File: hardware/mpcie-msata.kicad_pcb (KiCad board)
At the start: 4 copper layers, 100 x 85 mm, 205 parts, among them J102 TNG-Power-BTM, J103 TNG-Power-TOP, J104 TNG-Data-BTM, J105 TNG-Data-TOP, J201 Mini-PCIE, J202 SIM8060, J301 Mini-SATA, P101 Debug, P102 PE, Q301 40MHz, SW101 BOOT, U101 USB2514B, U102 LD1117, U103 TPS7A7002, U104 STM32F070CBT6, U105 82400152, U201 LM813, U301 TUSB9261PVP, U302 TLV71211DBVR, U303 AP7333-18SAG-7, U304 AT25DF011-SSHN-T, X101 24MHz, X102 TBD

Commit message: fix values
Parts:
- R114: value 510 -> 1k

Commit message: add hints
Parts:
- R310: value DNP -> 0
- R313: value 10k -> DNP
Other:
- board text added: "More distance to connector"
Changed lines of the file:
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@@
   (general
     (thickness 1.6)
-    (drawings 15)
+    (drawings 16)
     (tracks 2816)
     (zones 0)
@@
       (effects (font (size 0.2 0.2) (thickness 0.05)) (justify mirror))
     )
-    (fp_text value DNP (at 0 0.15 90) (layer B.Fab)
+    (fp_text value 0 (at 0 0.15 90) (layer B.Fab)
       (effects (font (size 0.2 0.2) (thickness 0.05)) (justify mirror))
     )
@@
       (effects (font (size 0.2 0.2) (thickness 0.05)) (justify mirror))
     )
-    (fp_text value 10k (at 0 0.15) (layer B.Fab)
+    (fp_text value DNP (at 0 0.15) (layer B.Fab)
       (effects (font (size 0.2 0.2) (thickness 0.05)) (justify mirror))
     )
@@
     )
   )
+  (gr_text "More distance to connector" (at 107.45 66.95) (layer Dwgs.User)
+    (effects (font (size 1.5 1.5) (thickness 0.3)))
+  )
   (gr_text "Mini SATA" (at 110.05 84.1 90) (layer F.SilkS)

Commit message: add version 1.1
 * fix footprints
 * remove lm813
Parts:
- removed C145: >100uF, ELKO_63
- removed C208: 10uF, C0805
- removed L104: 744230900, WE-CNSW-0603
- removed L110: INDUCTs, kicad-libraries:R0805E
- removed R107: DNP, R0402F
- removed R117: 10k, R0402F
- removed R205, R206, R207: 1k, kicad-libraries:R0402F
- removed RP202: 1k, kicad-libraries:4X0402
- removed U201: LM813, kicad-libraries:LM813
- added Q101: 2N7002, kicad-libraries:SOT23GDS, F.Cu at (104.2, 54.9)
- C148, C150, C151, C202: value >100uF -> 100uF
- C310, C311, C312, C313: footprint kicad-libraries:C0402E -> kicad-libraries:C0402F
- R111: value DNP -> 10k
- moved R106 12.5 mm to (105.7, 57.1)
- moved C129 11.7 mm to (105.1, 59.2)
- moved C127 11.7 mm to (102.4, 67.9)
- moved P101 11.7 mm to (99.8, 60.4)
- moved C123 11.7 mm to (93.0, 58.7)
- moved C130 11.7 mm to (97.0, 56.5)
- moved C131 11.7 mm to (94.0, 58.7)
- moved C124 11.7 mm to (93.5, 64.6)
- moved C133 11.7 mm to (93.9, 63.1)
- moved C137 11.7 mm to (89.4, 61.6)
- moved C138 11.7 mm to (91.5, 64.1)
- moved C139 11.7 mm to (90.0, 65.8)
- moved L108 11.7 mm to (93.2, 65.8)
- moved U104 11.7 mm to (99.5, 62.1)
- moved X102 11.7 mm to (91.5, 61.6)
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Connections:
- net Net-(R114-Pad2) renamed BOOT
- J102 pad 21: (no net) -> Net-(J102-Pad21)
- J102 pad 22: (no net) -> Net-(J102-Pad22)
- J102 pad 23: (no net) -> Net-(J102-Pad23)
- J102 pad 24: (no net) -> Net-(J102-Pad24)
- J102 pad 25: (no net) -> Net-(J102-Pad25)
- J102 pad 26: (no net) -> Net-(J102-Pad26)
- J102 pad 27: (no net) -> Net-(J102-Pad27)
- J102 pad 28: (no net) -> Net-(J102-Pad28)
- J102 pad 29: (no net) -> Net-(J102-Pad29)
- J102 pad 30: (no net) -> Net-(J102-Pad30)
- J103 pad 21: (no net) -> Net-(J103-Pad21)
- J103 pad 22: (no net) -> Net-(J103-Pad22)
- J103 pad 23: (no net) -> Net-(J103-Pad23)
- J103 pad 24: (no net) -> Net-(J103-Pad24)
- J103 pad 25: (no net) -> Net-(J103-Pad25)
- J103 pad 26: (no net) -> Net-(J103-Pad26)
- J103 pad 27: (no net) -> Net-(J103-Pad27)
- J103 pad 28: (no net) -> Net-(J103-Pad28)
- J103 pad 29: (no net) -> Net-(J103-Pad29)
- J103 pad 30: (no net) -> Net-(J103-Pad30)
- J105 pad 35: (no net) -> Net-(J105-Pad35)
- J105 pad 37: (no net) -> Net-(J105-Pad37)
- J201 pad 1: (no net) -> Net-(J201-Pad1)
- J201 pad 11: (no net) -> Net-(J201-Pad11)
- J201 pad 13: (no net) -> Net-(J201-Pad13)
- J201 pad 17: (no net) -> Net-(J201-Pad17)
- J201 pad 23: (no net) -> Net-(J201-Pad23)
- J201 pad 25: (no net) -> Net-(J201-Pad25)
- J201 pad 28: (no net) -> Net-(J201-Pad28)
- J201 pad 3: (no net) -> Net-(J201-Pad3)
- J201 pad 30: (no net) -> Net-(J201-Pad30)
- J201 pad 31: (no net) -> Net-(J201-Pad31)
- J201 pad 32: (no net) -> Net-(J201-Pad32)
- J201 pad 33: (no net) -> Net-(J201-Pad33)
- J201 pad 45: (no net) -> Net-(J201-Pad45)
- J201 pad 47: (no net) -> Net-(J201-Pad47)
- J201 pad 48: (no net) -> Net-(J201-Pad48)
- J201 pad 49: (no net) -> Net-(J201-Pad49)
- J201 pad 5: (no net) -> Net-(J201-Pad5)
- J201 pad 51: (no net) -> Net-(J201-Pad51)
- J201 pad 6: (no net) -> Net-(J201-Pad6)
- J201 pad 7: (no net) -> Net-(J201-Pad7)
- J301 pad 1: (no net) -> Net-(J301-Pad1)
- J301 pad 10: (no net) -> Net-(J301-Pad10)
- J301 pad 11: (no net) -> Net-(J301-Pad11)
- J301 pad 12: (no net) -> Net-(J301-Pad12)
- J301 pad 13: (no net) -> Net-(J301-Pad13)
- J301 pad 14: (no net) -> Net-(J301-Pad14)
- J301 pad 16: (no net) -> Net-(J301-Pad16)
- J301 pad 17: (no net) -> Net-(J301-Pad17)
- J301 pad 19: (no net) -> Net-(J301-Pad19)
- J301 pad 20: (no net) -> Net-(J301-Pad20)
- J301 pad 22: (no net) -> Net-(J301-Pad22)
- J301 pad 28: (no net) -> Net-(J301-Pad28)
- J301 pad 3: (no net) -> Net-(J301-Pad3)
- J301 pad 30: (no net) -> Net-(J301-Pad30)
- J301 pad 32: (no net) -> Net-(J301-Pad32)
- J301 pad 36: (no net) -> Net-(J301-Pad36)
- J301 pad 38: (no net) -> Net-(J301-Pad38)
- J301 pad 42: (no net) -> Net-(J301-Pad42)
- J301 pad 43: (no net) -> Net-(J301-Pad43)
- J301 pad 44: (no net) -> Net-(J301-Pad44)
- J301 pad 45: (no net) -> Net-(J301-Pad45)
- J301 pad 46: (no net) -> Net-(J301-Pad46)
- J301 pad 47: (no net) -> Net-(J301-Pad47)
- J301 pad 48: (no net) -> Net-(J301-Pad48)
- J301 pad 5: (no net) -> Net-(J301-Pad5)
- J301 pad 51: (no net) -> Net-(J301-Pad51)
- J301 pad 6: (no net) -> Net-(J301-Pad6)
- J301 pad 7: (no net) -> Net-(J301-Pad7)
- J301 pad 8: (no net) -> Net-(J301-Pad8)
- R109 pad 2: 3V3 -> GND
- RP201 pad 3: (no net) -> Net-(RP201-Pad3)
- RP201 pad 6: (no net) -> Net-(RP201-Pad6)
- RP301 pad 2: (no net) -> Net-(RP301-Pad2)
- RP301 pad 3: (no net) -> Net-(RP301-Pad3)
- RP301 pad 6: (no net) -> Net-(RP301-Pad6)
- RP301 pad 7: (no net) -> Net-(RP301-Pad7)
- U101 pad 12: (no net) -> Net-(U101-Pad12)
- U101 pad 16: (no net) -> Net-(U101-Pad16)
- U101 pad 18: (no net) -> Net-(U101-Pad18)
- U101 pad 20: (no net) -> Net-(U101-Pad20)
- U103 pad 5: (no net) -> Net-(U103-Pad5)
- U104 pad 10: LM813_LED_WL -> Net-(U104-Pad10)
- U104 pad 11: LM813_WLAN_DIS -> Net-(U104-Pad11)
- U104 pad 2: LM813_BT_DIS -> Net-(U104-Pad2)
- U104 pad 28: (no net) -> Net-(U104-Pad28)
- U104 pad 3: LM813_LED_BT -> Net-(U104-Pad3)
- U104 pad 38: (no net) -> Net-(U104-Pad38)
- U104 pad 39: (no net) -> Net-(U104-Pad39)
- U104 pad 4: LM813_BT_WAKE_HOST -> Net-(U104-Pad4)
- U104 pad 41: (no net) -> Net-(U104-Pad41)
- U104 pad 42: (no net) -> Net-(U104-Pad42)
- U104 pad 46: LM813_EN -> Net-(U104-Pad46)
- U104 pad 7: (no net) -> Net-(U104-Pad7)
- U301 pad 10: (no net) -> Net-(U301-Pad10)
- U301 pad 11: (no net) -> Net-(U301-Pad11)
- U301 pad 13: (no net) -> Net-(U301-Pad13)
- U301 pad 14: (no net) -> Net-(U301-Pad14)
- U301 pad 15: (no net) -> Net-(U301-Pad15)
- U301 pad 16: (no net) -> Net-(U301-Pad16)
- U301 pad 22: (no net) -> Net-(U301-Pad22)
- U301 pad 23: (no net) -> Net-(U301-Pad23)
- U301 pad 25: (no net) -> Net-(U301-Pad25)
- U301 pad 26: (no net) -> Net-(U301-Pad26)
- U301 pad 27: (no net) -> Net-(U301-Pad27)
- U301 pad 28: (no net) -> Net-(U301-Pad28)
- U301 pad 37: (no net) -> Net-(U301-Pad37)
- U301 pad 42: (no net) -> Net-(U301-Pad42)
- U301 pad 43: (no net) -> Net-(U301-Pad43)
- U301 pad 45: (no net) -> Net-(U301-Pad45)
- U301 pad 46: (no net) -> Net-(U301-Pad46)
- U301 pad 54: (no net) -> Net-(U301-Pad54)
- U301 pad 64: (no net) -> Net-(U301-Pad64)
- U301 pad 8: (no net) -> Net-(U301-Pad8)
- U301 pad 9: (no net) -> Net-(U301-Pad9)
- U302 pad 4: (no net) -> Net-(U302-Pad4)
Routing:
- net 5V: track 162.2 -> 0.00 mm, vias 12 -> 0
- net 3V3: track 212.6 -> 101.5 mm, vias 31 -> 29
- net LM813_DM: track 39.6 -> 0.00 mm, vias 1 -> 0
- net LM813_DP: track 37.1 -> 0.00 mm, vias 1 -> 0
- net LM813_EN: track 30.6 -> 0.00 mm, vias 2 -> 0
- net LM813_WLAN_DIS: track 26.5 -> 0.00 mm, vias 2 -> 0
- net LM813_BT_DIS: track 24.6 -> 0.00 mm, vias 2 -> 0
- net Net-(RP202-Pad3): track 20.4 -> 0.00 mm, vias 1 -> 0
- net LM813_LED_BT: track 15.4 -> 0.00 mm, vias 1 -> 0
- net GND: track 389.5 -> 374.7 mm, vias 285 -> 270
- net MPCIE_LED_WPAN: track 34.9 -> 49.0 mm
- net MPCIE_LED_WWAN: track 34.7 -> 48.7 mm
- net MPCIE_LED_WIFI: track 34.8 -> 48.8 mm
- net MSATA_TX: track 41.4 -> 55.2 mm
- net MPCIE_#RESET: track 52.4 -> 66.2 mm
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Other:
- board text added: "Copyright Tinkerforge GmbH 2020. This documentation describes Open Hardware and is licensed under the CERN OHL v. 1.1. You may redistribute and modify this documentation under the terms of the CERN OHL v.1.1. (http://ohwr.org/cernohl). This documentation is distributed WITHOUT ANY EXPRESS OR IMPLIED WARRANTY, INCLUDING OF MERCHANTABILITY, SATISFACTORY QUALITY AND FITNESS FOR A PARTICULAR PURPOSE.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"
- board text added: "MPCIE-MSATA REV 1.1"
- board text removed: "MPCIE-MSATA-WIFI/BT REV 1.0"
- board text removed: "More distance to connector"

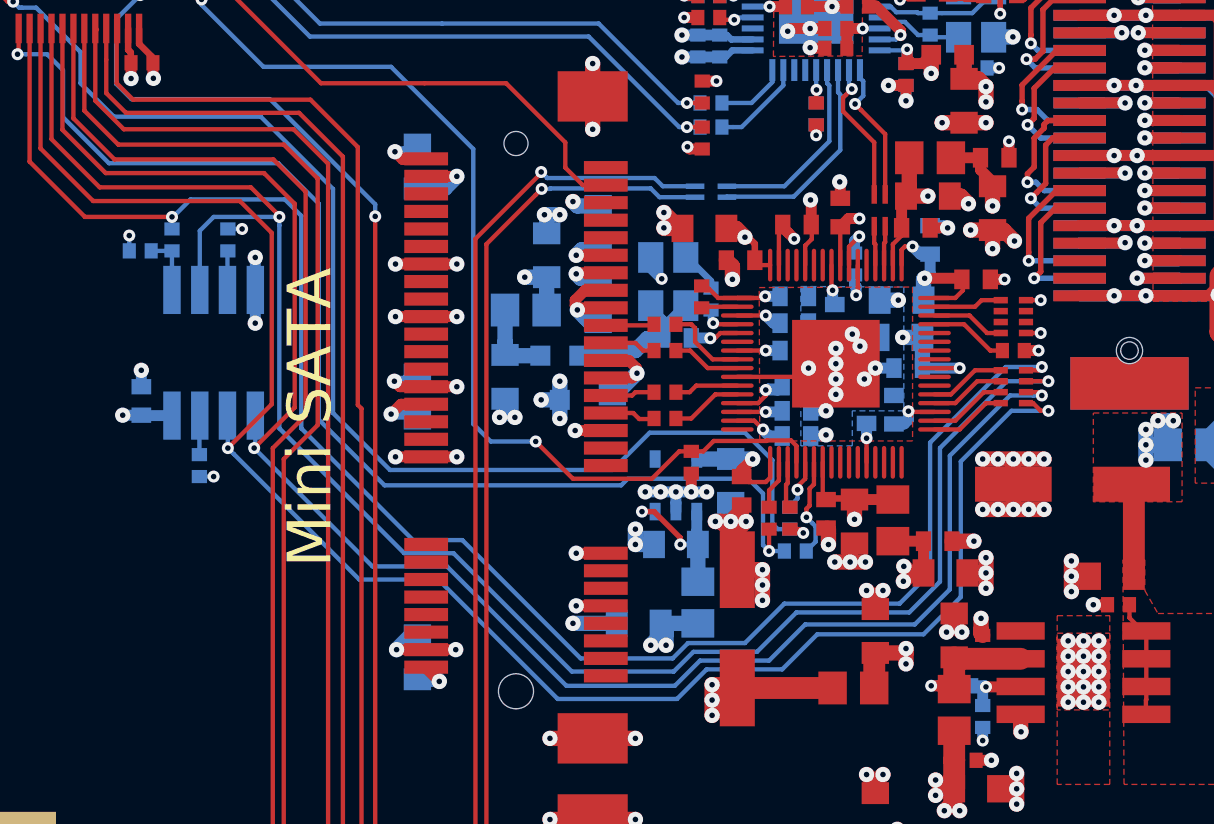
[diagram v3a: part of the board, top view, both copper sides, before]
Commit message: fix footprints
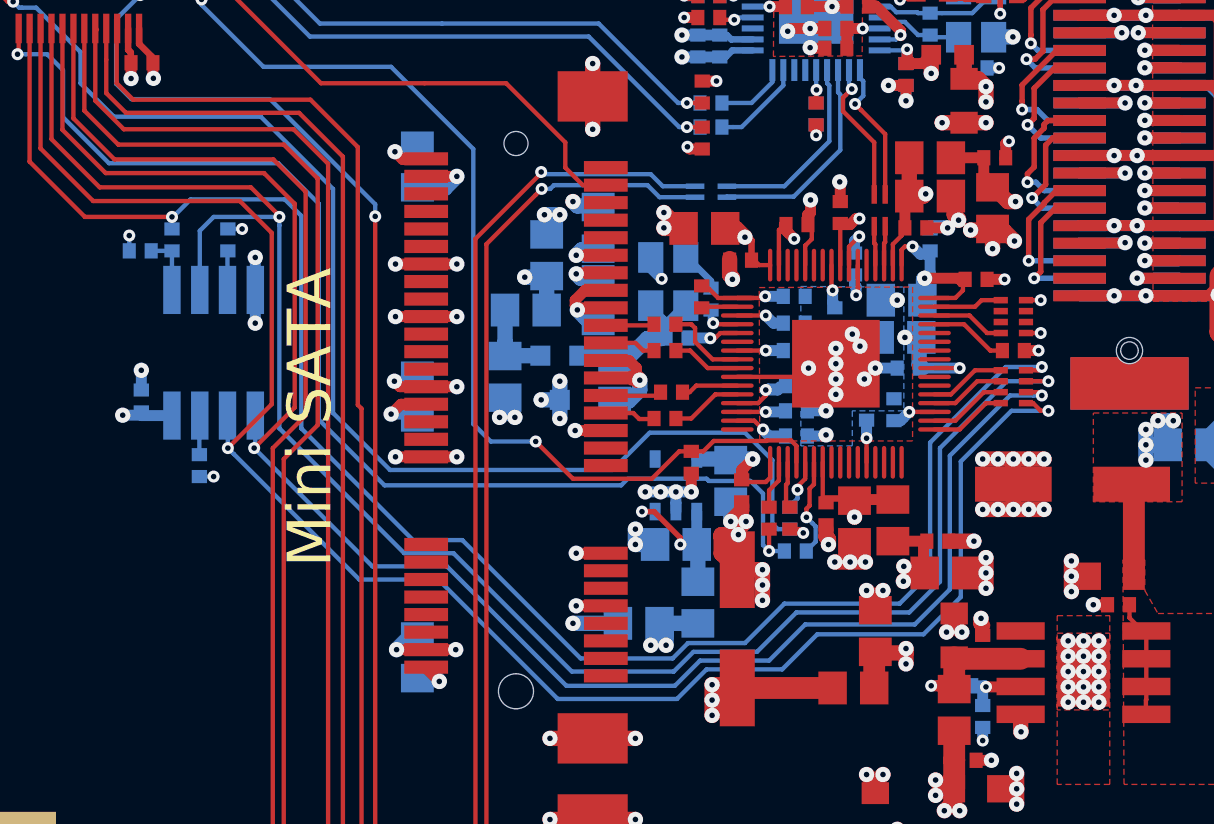
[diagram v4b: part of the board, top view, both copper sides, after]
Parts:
- C121, C122: value TBD/47pF -> 47pF
- C137, C138: value TBD -> 33pF
- C301, C302, C303, C304, C305, C309, C325, C326, C327, C328, C329, C330, C331, C339, C340, C341, C342, C345, C346: footprint C0805 -> kicad-libraries:C0805E
- C306: value >100uF -> 100uF
- C308, C314, C315, C316, C317, C318, C319, C320, C321, C322, C323, C324, C332, C333, C334, C335, C336, C337, C338, C343, C344, C347: footprint kicad-libraries:C0402E -> kicad-libraries:C0402F
- X102: value TBD -> 8MHz
- moved C326 0.36 mm to (124.0, 82.4)
- moved C312 0.30 mm to (126.5, 83.0)
- moved C342 0.10 mm to (138.3, 74.0)
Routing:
- net GND: track 374.7 -> 374.2 mm, vias 270 -> 269

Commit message: fix name
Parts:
- U304: value AT25DF011-SSHN-T -> AT25DF011-SSHN-T

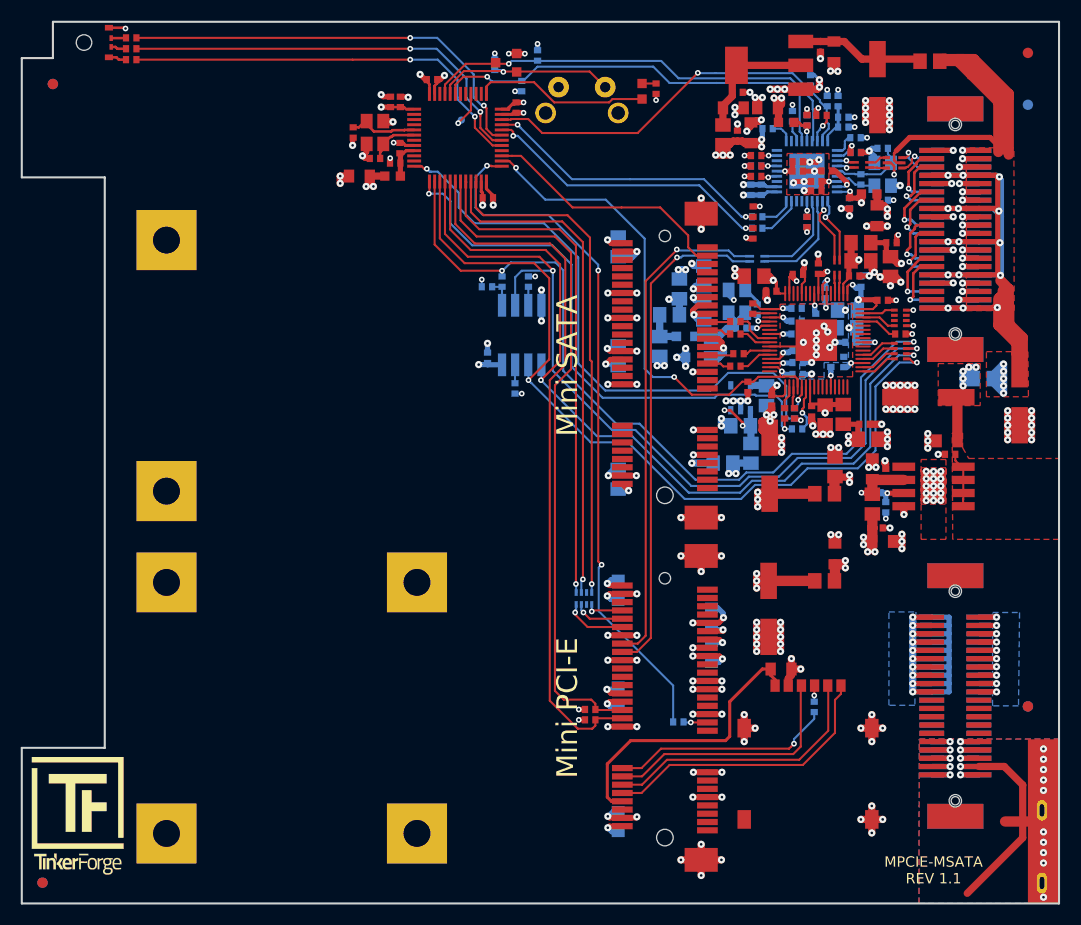
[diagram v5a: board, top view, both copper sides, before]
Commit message: fix footprints
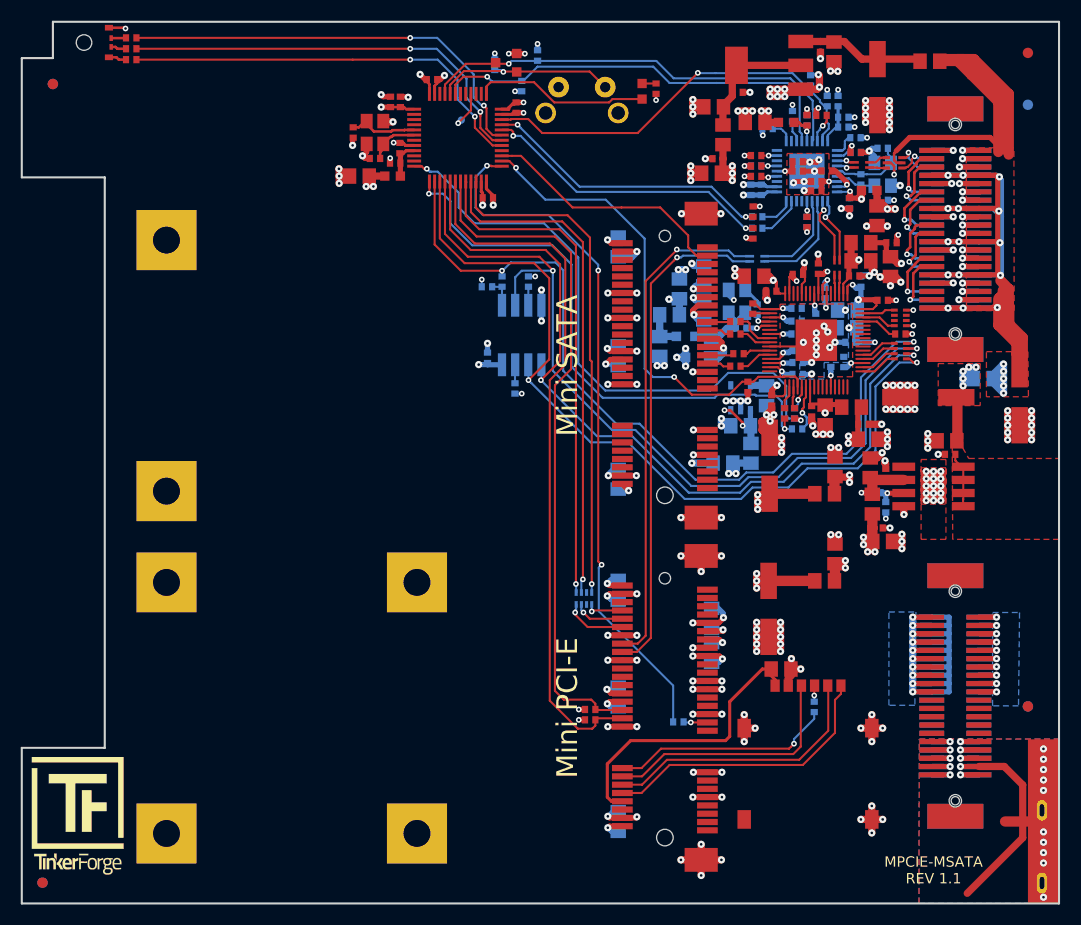
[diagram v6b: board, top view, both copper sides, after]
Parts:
- C116, C125, C128, C132, C136, C139, C140, C146, C147, C201, C203, C204, C205, C206, C207, C209: footprint C0805 -> kicad-libraries:C0805E
- moved C128 5.45 mm to (124.0, 65.5), turned to 180 degrees
- moved C134 2.91 mm to (124.5, 64.2), turned to 180 degrees
- moved C136 1.90 mm to (124.2, 59.1), turned to 180 degrees
- moved C116 1.84 mm to (128.2, 60.6)
- moved L304 1.06 mm to (137.4, 88.1), turned to 180 degrees
- moved L103 0.35 mm to (139.2, 67.2)
- moved C140 0.22 mm to (139.2, 94.0)
- moved C343 0.10 mm to (138.6, 89.8)
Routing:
- net GND: track 374.2 -> 379.8 mm, vias 269 -> 275
- net 3V3: track 101.5 -> 98.5 mm, vias 29 -> 28

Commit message: fix names
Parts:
- U302: value TLV71211DBVR -> TLV71211DBVR
- U303: value AP7333-18SAG-7 -> AP7333-18SAG-7

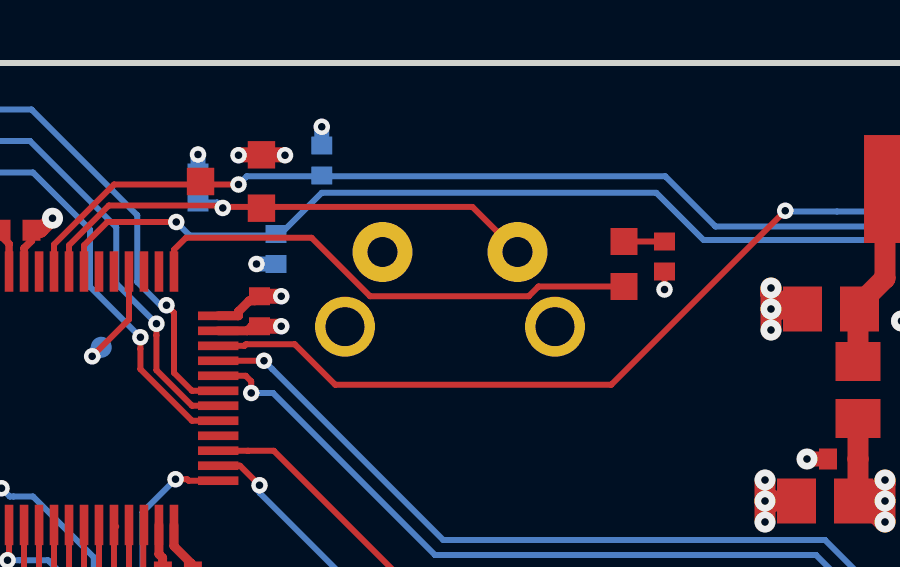
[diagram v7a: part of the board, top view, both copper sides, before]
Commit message: all footprints updated
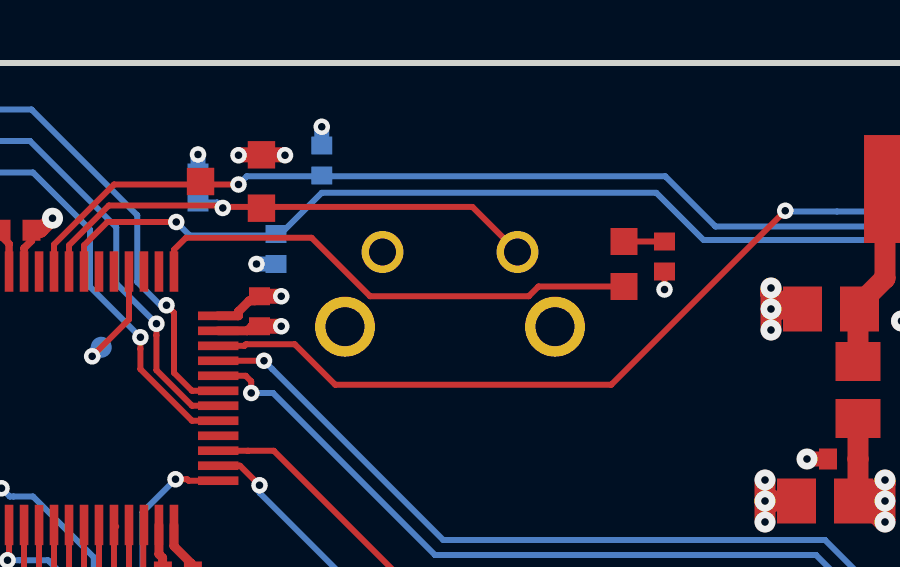
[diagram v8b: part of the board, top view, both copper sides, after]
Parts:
- C101, C102, C103, C104, C105, C106, C107, C108, C109, C110, C111, C112, C113, C114, C115, C117, C118, C119, C120, C121, C122, C123, C124, C126, C127, C129, C130, C131, C133, C134, C135, C137, C138, C141, C142, C143, C144: footprint C0402F -> kicad-libraries:C0402F
- C148, C150, C151, C202, C306: footprint ELKO_63 -> kicad-libraries:ELKO_63
- D102: footprint D0603F -> kicad-libraries:D0603F
- J102, J104: footprint TNG-40-BTM -> kicad-libraries:TNG-40-BTM
- J103, J105: footprint TNG-40-TOP -> kicad-libraries:TNG-40-TOP
- L101, L103, L108: footprint R0603F -> kicad-libraries:R0603F
- L102, L105: footprint WE-CNSW-0603 -> kicad-libraries:WE-CNSW-0603
- LED101: footprint LED-RGB-LP -> kicad-libraries:LED-RGB-LP
- R101, R102, R103, R104, R105, R106, R108, R109, R110, R111, R112, R113, R114, R115, R116, R118, R119, R120, R121, R122, R123, R124: footprint R0402F -> kicad-libraries:R0402F
- U105: footprint SOT563-SPEC -> kicad-libraries:SOT563-SPEC
- X101: footprint CRYSTAL_3225 -> kicad-libraries:CRYSTAL_3225
